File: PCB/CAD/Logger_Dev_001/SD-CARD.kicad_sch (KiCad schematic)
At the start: 1 part, among them J1 Micro_SD_Card_Det2

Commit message: Library Submodule Update
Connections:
- net SDIO_DATA2_SDCARD: now reaches J1.1 (DAT2)
- net GND: now reaches J1.11 (SHIELD)
- net GND: now also J1.6 (VSS)
- net SDIO_DATA3_SDCARD: now reaches J1.2 (DAT3/CD)
- net SDIO_CMD_SDCARD: now reaches J1.3 (CMD)
- net 3v3_VCC: now reaches J1.4 (VDD)
- net SDIO_CLK_SDCARD: now reaches J1.5 (CLK)
- net SDIO_DATA0_SDCARD: now reaches J1.7 (DAT0)
- net SDIO_DATA1_SDCARD: now reaches J1.8 (DAT1)
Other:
- moved on the sheet: J1

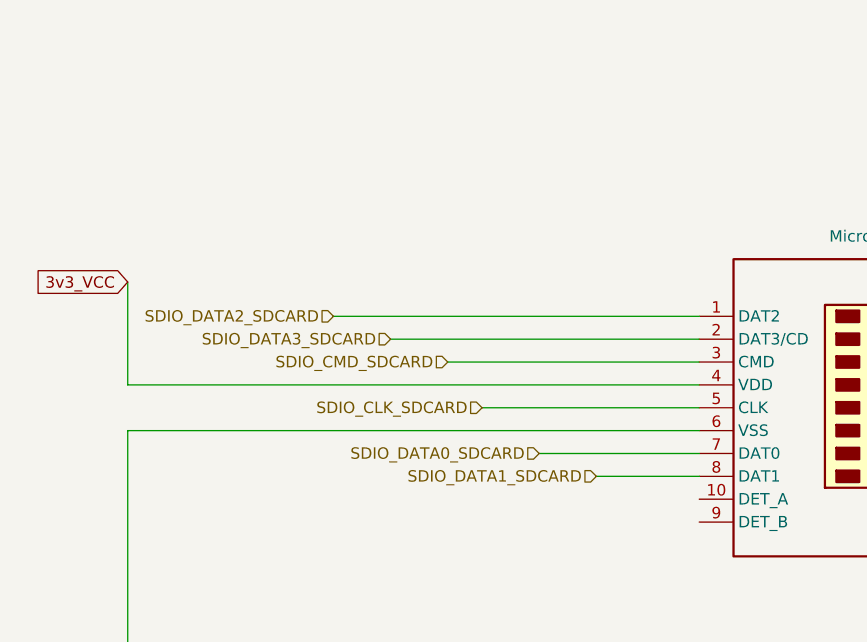
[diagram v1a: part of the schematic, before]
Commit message: Power input Schematic
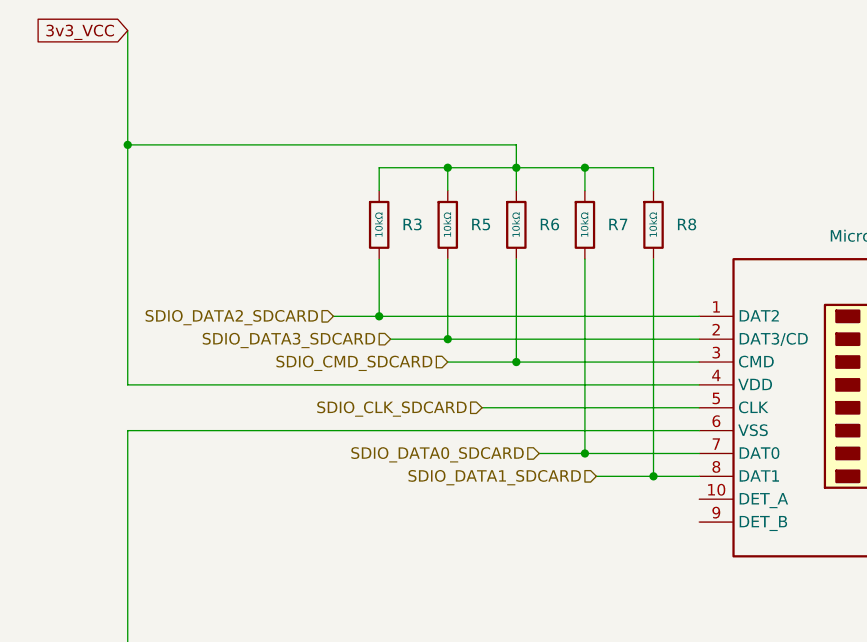
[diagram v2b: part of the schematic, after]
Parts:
- added R3, R5, R6, R7, R8: 10kΩ, PCM_JLCPCB:R_0402, symbol PCM_JLCPCB-Resistors:0402,10kΩ
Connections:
- net 3v3_VCC: now also R3.1, R5.1, R6.1, R7.1, R8.1
- net SDIO_CMD_SDCARD: now also R6.2
- net SDIO_DATA0_SDCARD: now also R7.2
- net SDIO_DATA1_SDCARD: now also R8.2
- net SDIO_DATA2_SDCARD: now also R3.2
- net SDIO_DATA3_SDCARD: now also R5.2

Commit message: Updated Schematic
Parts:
- added TP10: CMD, symbol Connector:TestPoint
- added TP11: DAT3/CD, symbol Connector:TestPoint
- added TP12: DAT2, symbol Connector:TestPoint
- added TP7: DAT1, symbol Connector:TestPoint
- added TP8: DAT0, symbol Connector:TestPoint
- added TP9: CLK, symbol Connector:TestPoint
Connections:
- net SDIO_CLK_SDCARD renamed !SDIO_CLK_SDCARD
- net !SDIO_CLK_SDCARD: now also TP9.1
- net SDIO_CMD_SDCARD renamed !SDIO_CMD_SDCARD
- net !SDIO_CMD_SDCARD: now also TP10.1
- net SDIO_DATA0_SDCARD renamed !SDIO_DATA0_SDCARD
- net !SDIO_DATA0_SDCARD: now also TP8.1
- net SDIO_DATA1_SDCARD renamed !SDIO_DATA1_SDCARD
- net !SDIO_DATA1_SDCARD: now also TP7.1
- net SDIO_DATA2_SDCARD renamed !SDIO_DATA2_SDCARD
- net !SDIO_DATA2_SDCARD: now also TP12.1
- net SDIO_DATA3_SDCARD renamed !SDIO_DATA3_SDCARD
- net !SDIO_DATA3_SDCARD: now also TP11.1
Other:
- company: (none) -> Jake Odgers
- title: (none) -> Mileage Logger
- moved on the sheet: J1, R3, R5, R6, R7, R8

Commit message: Schematic finalised
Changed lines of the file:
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@@
 		(company "Jake Odgers")
+	)
+	(text_box "SDIO to SDCARD\n"
+		(exclude_from_sim no)
+		(at 38.1 36.83 0)
+		(size 227.33 114.3)
+		(margins 0.9525 0.9525 0.9525 0.9525)
+		(stroke
+			(width 0)
+			(type solid)
+		)
+		(fill
+			(type none)
+		)
+		(effects
+			(font
+				(size 2.54 2.54)
+			)
+			(justify left top)
+		)
 	)
 	(junction

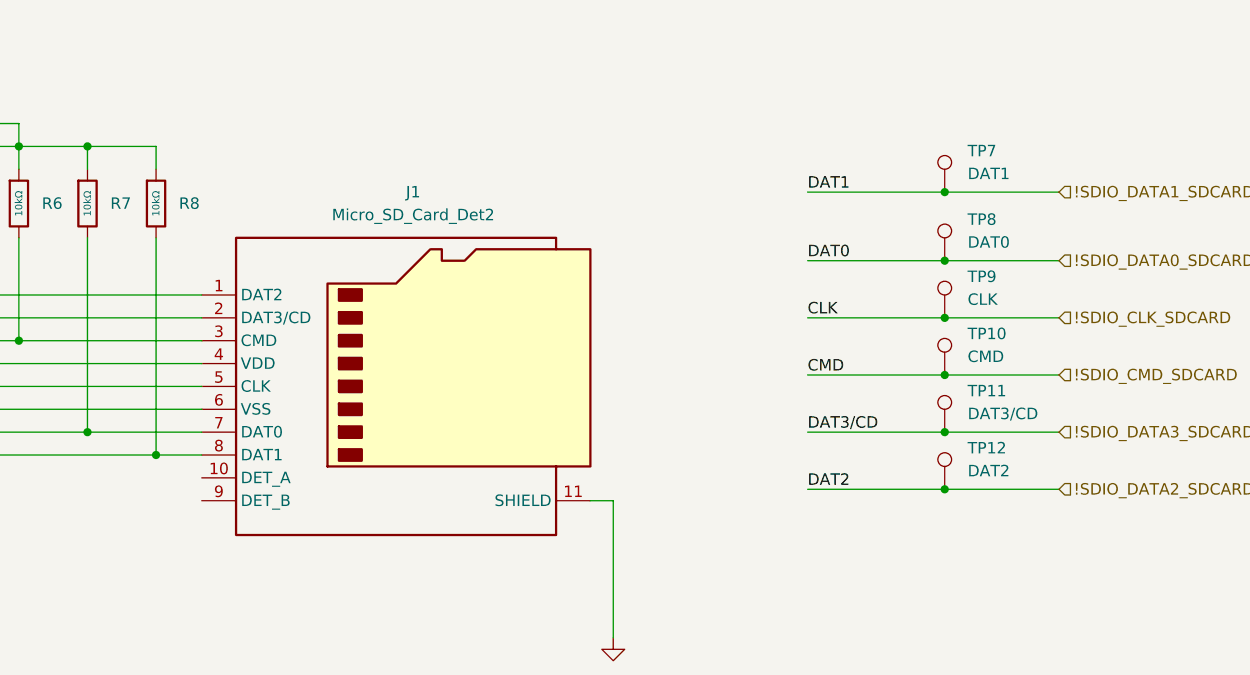
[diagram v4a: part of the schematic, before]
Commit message: Update some footprints
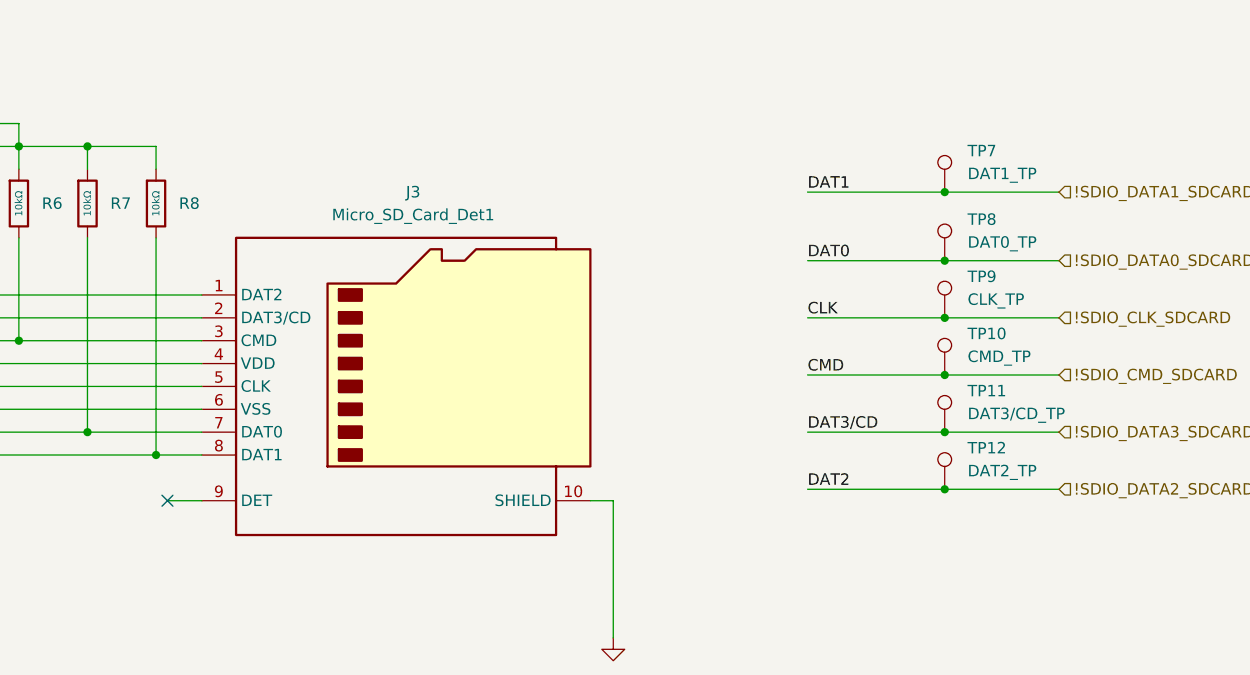
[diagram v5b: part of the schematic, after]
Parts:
- removed J1: Micro_SD_Card_Det2, symbol Connector:Micro_SD_Card_Det2
- added J3: Micro_SD_Card_Det1, symbol Connector:Micro_SD_Card_Det1
- TP10: value CMD -> CMD_TP
- TP11: value DAT3/CD -> DAT3/CD_TP
- TP12: value DAT2 -> DAT2_TP
- TP7: value DAT1 -> DAT1_TP
- TP8: value DAT0 -> DAT0_TP
- TP9: value CLK -> CLK_TP
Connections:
- net !SDIO_CLK_SDCARD: now also J3.5 (CLK)
- net !SDIO_CMD_SDCARD: now also J3.3 (CMD)
- net !SDIO_DATA0_SDCARD: now also J3.7 (DAT0)
- net !SDIO_DATA1_SDCARD: now also J3.8 (DAT1)
- net !SDIO_DATA2_SDCARD: now also J3.1 (DAT2)
- net !SDIO_DATA3_SDCARD: now also J3.2 (DAT3/CD)
- net 3v3_VCC: now also J3.4 (VDD)
- net GND: now also J3.10 (SHIELD), J3.6 (VSS)
- no-connect marks 0 -> 1
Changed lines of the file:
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@@
 		(color 0 0 0 0)
 	)
+	(no_connect
+		(at 123.19 109.22)
+	)
 	(wire
 		(pts
@@
 		(pts
 			(xy 91.44 69.85) (xy 99.06 69.85)
+		)
+		(stroke
+			(width 0)
+			(type default)
+		)
+	)
+	(wire
+		(pts
+			(xy 123.19 109.22) (xy 127 109.22)
 		)
 		(stroke
@@
 			)
 		)
-		(property "Value" "DAT0"
+		(property "Value" "DAT0_TP"
 			(at 212.09 80.5179 0)
 			(effects
@@
 			)
 		)
-		(property "Value" "DAT1"
+		(property "Value" "DAT1_TP"
 			(at 212.09 72.8979 0)
 			(effects
@@
 			)
 		)
-		(property "Value" "DAT3/CD"
+		(property "Value" "DAT3/CD_TP"
 			(at 212.09 99.5679 0)
 			(effects
@@
 			)
 		)
-		(property "Value" "CLK"
+		(property "Value" "CLK_TP"
 			(at 212.09 86.8679 0)
 			(effects
@@
 			)
 		)
-		(property "Value" "DAT2"
+		(property "Value" "DAT2_TP"
 			(at 212.09 105.9179 0)
 			(effects
@@
 				(path "/9546b831-c7ee-4f40-8993-5fd5a38d4078/3ed175c0-d86e-4c50-b284-622e335d2432"
 					(reference "TP12")
-					(unit 1)
-				)
-			)
-		)
-	)
-	(symbol
-		(lib_id "Connector:Micro_SD_Card_Det2")
-		(at 149.86 96.52 0)
-		(unit 1)
-		(exclude_from_sim no)
-		(in_bom yes)
-		(on_board yes)
-		(dnp no)
-		(fields_autoplaced yes)
-		(property "Reference" "J1"
-			(at 150.495 74.93 0)
-			(effects
-				(font
-					(size 1.27 1.27)
-				)
-			)
-		)
-		(property "Value" "Micro_SD_Card_Det2"
-			(at 150.495 77.47 0)
-			(effects
-				(font
-					(size 1.27 1.27)
-				)
-			)
-		)
-		(property "Footprint" ""
-			(at 201.93 78.74 0)
-			(effects
-				(font
-					(size 1.27 1.27)
-				)
-				(hide yes)
-			)
-		)
-		(property "Datasheet" "https://www.hirose.com/en/product/document?clcode=&productname=&series=DM3&documenttype=Catalog&lang=en&documentid=D49662_en"
-			(at 152.4 93.98 0)
-			(effects
-				(font
-					(size 1.27 1.27)
-				)
-				(hide yes)
-			)
-		)
-		(property "Description" "Micro SD Card Socket with two card detection pins"
-			(at 149.86 96.52 0)
-			(effects
-				(font
-					(size 1.27 1.27)
-				)
-				(hide yes)
-			)
-		)
-		(pin "1"
-		)
-		(pin "6"
-		)
-		(pin "4"
-		)
-		(pin "5"
-		)
-		(pin "2"
-		)
-		(pin "3"
-		)
-		(pin "7"
-		)
-		(pin "10"
-		)
-		(pin "9"
-		)
-		(pin "8"
-		)
-		(pin "11"
-		)
-		(instances
-			(project "Logger_Dev_001"
-				(path "/9546b831-c7ee-4f40-8993-5fd5a38d4078/3ed175c0-d86e-4c50-b284-622e335d2432"
-					(reference "J1")
 					(unit 1)
 				)
@@
 			)
 		)
-		(property "Value" "CMD"
+		(property "Value" "CMD_TP"
 			(at 212.09 93.2179 0)
 			(effects
@@
 					(unit 1)
 				)
+			)
+		)
+	)
+	(symbol
+		(lib_id "Connector:Micro_SD_Card_Det1")
+		(at 149.86 96.52 0)
+		(unit 1)
+		(exclude_from_sim no)
+		(in_bom yes)
+		(on_board yes)
+		(dnp no)
+		(fields_autoplaced yes)
+		(property "Reference" "J3"
+			(at 150.495 74.93 0)
+			(effects
+				(font
+					(size 1.27 1.27)
+				)
+			)
+		)
+		(property "Value" "Micro_SD_Card_Det1"
+			(at 150.495 77.47 0)
+			(effects
+				(font
+					(size 1.27 1.27)
+				)
+			)
+		)
+		(property "Footprint" ""
+			(at 201.93 78.74 0)
+			(effects
+				(font
+					(size 1.27 1.27)
+				)
+				(hide yes)
+			)
+		)
+		(property "Datasheet" "https://datasheet.lcsc.com/lcsc/2110151630_XKB-Connectivity-XKTF-015-N_C381082.pdf"
+			(at 149.86 93.98 0)
+			(effects
+				(font
+					(size 1.27 1.27)
+				)
+				(hide yes)
+			)
+		)
+		(property "Description" "Micro SD Card Socket with one card detection pin"
+			(at 149.86 96.52 0)
+			(effects
+				(font
+					(size 1.27 1.27)
+				)
+				(hide yes)
+			)
+		)
+		(pin "10"
+		)
+		(pin "2"
+		)
+		(pin "4"
+		)
+		(pin "3"
+		)
+		(pin "1"
+		)
+		(pin "8"
+		)
+		(pin "7"
+		)
+		(pin "5"
+		)
+		(pin "6"
+		)
+		(pin "9"
+		)
+		(instances
+			(project ""
+				(path "/9546b831-c7ee-4f40-8993-5fd5a38d4078/3ed175c0-d86e-4c50-b284-622e335d2432"
+					(reference "J3")
+					(unit 1)
+				)

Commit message: Schematic Finished
Still need to check BOM
Starting to layout PCB
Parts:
- J3: footprint (none) -> SD Card:J_SD_Card-micro_socket_A
- TP10, TP11, TP12, TP7, TP8, TP9: footprint (none) -> TestPoint:TestPoint_Pad_D2.5mm
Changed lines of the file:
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@@
 			)
 		)
-		(property "Footprint" ""
+		(property "Footprint" "TestPoint:TestPoint_Pad_D2.5mm"
 			(at 214.63 82.55 0)
 			(effects
@@
 			)
 		)
-		(property "Footprint" ""
+		(property "Footprint" "TestPoint:TestPoint_Pad_D2.5mm"
 			(at 214.63 74.93 0)
 			(effects
@@
 			)
 		)
-		(property "Footprint" ""
+		(property "Footprint" "TestPoint:TestPoint_Pad_D2.5mm"
 			(at 214.63 101.6 0)
 			(effects
@@
 			)
 		)
-		(property "Footprint" ""
+		(property "Footprint" "TestPoint:TestPoint_Pad_D2.5mm"
 			(at 214.63 88.9 0)
 			(effects
@@
 			)
 		)
-		(property "Footprint" ""
+		(property "Footprint" "TestPoint:TestPoint_Pad_D2.5mm"
 			(at 214.63 107.95 0)
 			(effects
@@
 			)
 		)
-		(property "Footprint" ""
+		(property "Footprint" "TestPoint:TestPoint_Pad_D2.5mm"
 			(at 214.63 95.25 0)
 			(effects
@@
 			)
 		)
-		(property "Footprint" ""
+		(property "Footprint" "SD Card:J_SD_Card-micro_socket_A"
 			(at 201.93 78.74 0)
 			(effects

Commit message: Update via size to reduce cost
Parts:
- J3: LCSC (none) -> C22467599
- TP10, TP11, TP12, TP7, TP8, TP9: now left out of the parts list
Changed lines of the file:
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@@
 		(unit 1)
 		(exclude_from_sim no)
-		(in_bom yes)
+		(in_bom no)
 		(on_board yes)
 		(dnp no)
@@
 		(unit 1)
 		(exclude_from_sim no)
-		(in_bom yes)
+		(in_bom no)
 		(on_board yes)
 		(dnp no)
@@
 		(unit 1)
 		(exclude_from_sim no)
-		(in_bom yes)
+		(in_bom no)
 		(on_board yes)
 		(dnp no)
@@
 		(unit 1)
 		(exclude_from_sim no)
-		(in_bom yes)
+		(in_bom no)
 		(on_board yes)
 		(dnp no)
@@
 		(unit 1)
 		(exclude_from_sim no)
-		(in_bom yes)
+		(in_bom no)
 		(on_board yes)
 		(dnp no)
@@
 		(unit 1)
 		(exclude_from_sim no)
-		(in_bom yes)
+		(in_bom no)
 		(on_board yes)
 		(dnp no)
@@
 			(at 149.86 96.52 0)
 			(effects
+				(font
+					(size 1.27 1.27)
+				)
+				(hide yes)
+			)
+		)
+		(property "LCSC" "C22467599"
+			(at 149.86 96.52 0)
+			(effects
